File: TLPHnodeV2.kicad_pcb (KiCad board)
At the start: 4 copper layers, 28 x 20.5 mm, 34 parts, among them P3 USB (power only), SW1 Reset, U1 NCP703, U2 LD39130S, U3 LPS25HB, U4 Si7006-A20, U5 ESP-12E, U6 ISL29035, U7 bq25070

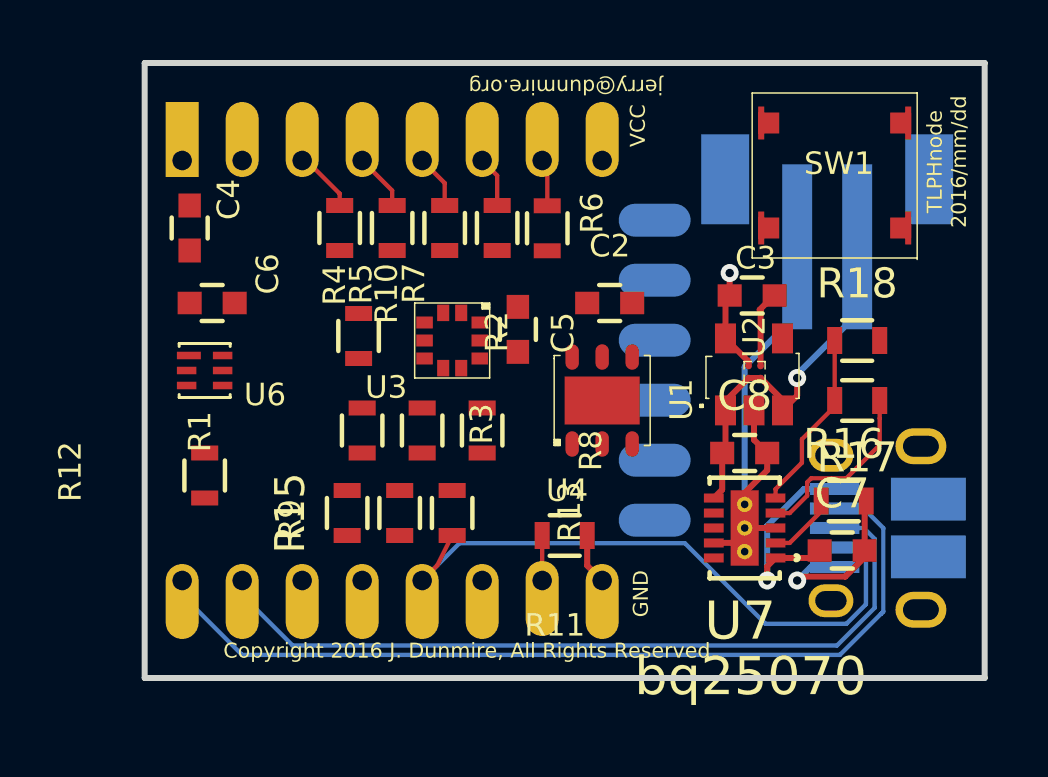
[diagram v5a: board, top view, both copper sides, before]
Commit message: CP - signals routed
On branch master
modified:   TLPHnodeV2.kicad_pcb
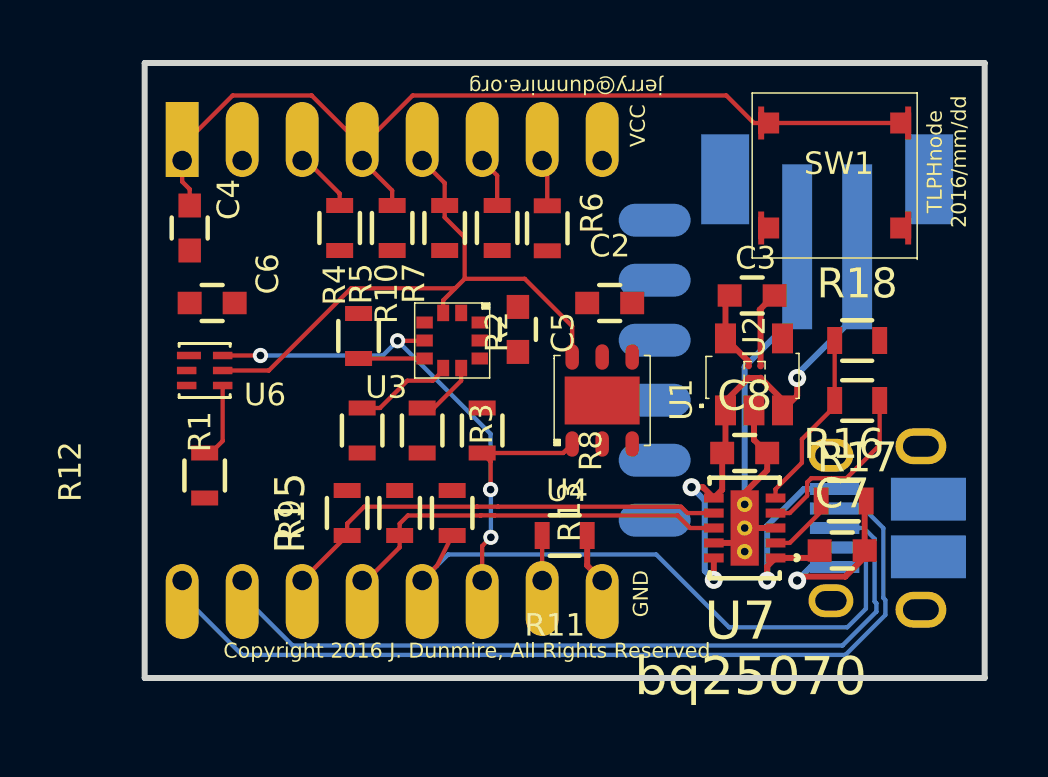
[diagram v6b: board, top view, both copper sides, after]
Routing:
- net Net-(C4-Pad1): track 1.91 -> 30.9 mm
- net /node/I2C_SDA: track 0.00 -> 20.8 mm, vias 0 -> 4
- net /node/I2C_SCL: track 1.81 -> 20.1 mm
- net /node/CTRL: track 0.14 -> 15.2 mm
- net /node/CHRG: track 0.00 -> 13.3 mm
- net +BATT: track 12.8 -> 17.8 mm, vias 1 -> 3
- net Net-(R1-Pad2): track 0.00 -> 3.29 mm
- net Net-(R12-Pad2): track 0.00 -> 2.62 mm
- net Net-(R2-Pad2): track 0.00 -> 2.20 mm
- net Net-(R3-Pad2): track 0.00 -> 2.10 mm
- net VCC: track 3.48 -> 2.73 mm, vias 1 -> 0
